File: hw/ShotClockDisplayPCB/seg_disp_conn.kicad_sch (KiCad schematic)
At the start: 4 parts, among them J2 Conn_01x05_Socket, J3 Conn_01x05_Socket, J4 Conn_01x05_Socket, J5 Conn_01x05_Socket

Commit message: Finshed both schematics
- LED driving transistors are placed
- All connectors on segment display PCB are placed
- All schematic references have been re-configured (autosort on Y axis)
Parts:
- renumbered J4 to J3, J3 to J4
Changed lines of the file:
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@@
       (project "ShotClockDisplayPCB"
         (path "/baf3f1b3-1588-4756-b7d1-50b7c58bafb0/06b39ac0-a89e-4700-88fa-059ca62688ec"
-          (reference "#PWR03") (unit 1)
+          (reference "#PWR025") (unit 1)
         )
       )
@@
       (project "ShotClockDisplayPCB"
         (path "/baf3f1b3-1588-4756-b7d1-50b7c58bafb0/06b39ac0-a89e-4700-88fa-059ca62688ec"
-          (reference "#PWR04") (unit 1)
+          (reference "#PWR026") (unit 1)
         )
       )
@@
   (symbol (lib_id "Connector:Conn_01x05_Socket") (at 180.34 80.01 0) (unit 1)
     (in_bom yes) (on_board yes) (dnp no)
-    (property "Reference" "J4" (at 181.61 78.74 0)
+    (property "Reference" "J3" (at 181.61 78.74 0)
       (effects (font (size 1.27 1.27)) (justify left))
     )
@@
       (project "ShotClockDisplayPCB"
         (path "/baf3f1b3-1588-4756-b7d1-50b7c58bafb0/06b39ac0-a89e-4700-88fa-059ca62688ec"
-          (reference "J4") (unit 1)
+          (reference "J3") (unit 1)
         )
       )
@@
   (symbol (lib_id "Connector:Conn_01x05_Socket") (at 118.11 97.79 0) (unit 1)
     (in_bom yes) (on_board yes) (dnp no)
-    (property "Reference" "J3" (at 119.38 96.52 0)
+    (property "Reference" "J4" (at 119.38 96.52 0)
       (effects (font (size 1.27 1.27)) (justify left))
     )
@@
       (project "ShotClockDisplayPCB"
         (path "/baf3f1b3-1588-4756-b7d1-50b7c58bafb0/06b39ac0-a89e-4700-88fa-059ca62688ec"
-          (reference "J3") (unit 1)
+          (reference "J4") (unit 1)
         )
       )

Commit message: Display print
Changed mainboard connector to FPC connector
Created routing for board
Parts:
- renumbered J2 to J1, J3 to J2, J4 to J3, J5 to J4
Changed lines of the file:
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@@
   (symbol (lib_id "Connector:Conn_01x05_Socket") (at 118.11 80.01 0) (unit 1)
     (in_bom yes) (on_board yes) (dnp no)
-    (property "Reference" "J2" (at 119.38 78.74 0)
+    (property "Reference" "J1" (at 119.38 78.74 0)
       (effects (font (size 1.27 1.27)) (justify left))
     )
@@
       (project "ShotClockDisplayPCB"
         (path "/baf3f1b3-1588-4756-b7d1-50b7c58bafb0/06b39ac0-a89e-4700-88fa-059ca62688ec"
-          (reference "J2") (unit 1)
+          (reference "J1") (unit 1)
         )
       )
@@
   (symbol (lib_id "Connector:Conn_01x05_Socket") (at 180.34 80.01 0) (unit 1)
     (in_bom yes) (on_board yes) (dnp no)
-    (property "Reference" "J3" (at 181.61 78.74 0)
+    (property "Reference" "J2" (at 181.61 78.74 0)
       (effects (font (size 1.27 1.27)) (justify left))
     )
@@
       (project "ShotClockDisplayPCB"
         (path "/baf3f1b3-1588-4756-b7d1-50b7c58bafb0/06b39ac0-a89e-4700-88fa-059ca62688ec"
-          (reference "J3") (unit 1)
+          (reference "J2") (unit 1)
         )
       )
@@
   (symbol (lib_id "Connector:Conn_01x05_Socket") (at 180.34 97.79 0) (unit 1)
     (in_bom yes) (on_board yes) (dnp no)
-    (property "Reference" "J5" (at 181.61 96.52 0)
+    (property "Reference" "J4" (at 181.61 96.52 0)
       (effects (font (size 1.27 1.27)) (justify left))
     )
@@
       (project "ShotClockDisplayPCB"
         (path "/baf3f1b3-1588-4756-b7d1-50b7c58bafb0/06b39ac0-a89e-4700-88fa-059ca62688ec"
-          (reference "J5") (unit 1)
+          (reference "J4") (unit 1)
         )
       )
@@
   (symbol (lib_id "Connector:Conn_01x05_Socket") (at 118.11 97.79 0) (unit 1)
     (in_bom yes) (on_board yes) (dnp no)
-    (property "Reference" "J4" (at 119.38 96.52 0)
+    (property "Reference" "J3" (at 119.38 96.52 0)
       (effects (font (size 1.27 1.27)) (justify left))
     )
@@
       (project "ShotClockDisplayPCB"
         (path "/baf3f1b3-1588-4756-b7d1-50b7c58bafb0/06b39ac0-a89e-4700-88fa-059ca62688ec"
-          (reference "J4") (unit 1)
+          (reference "J3") (unit 1)
         )
       )

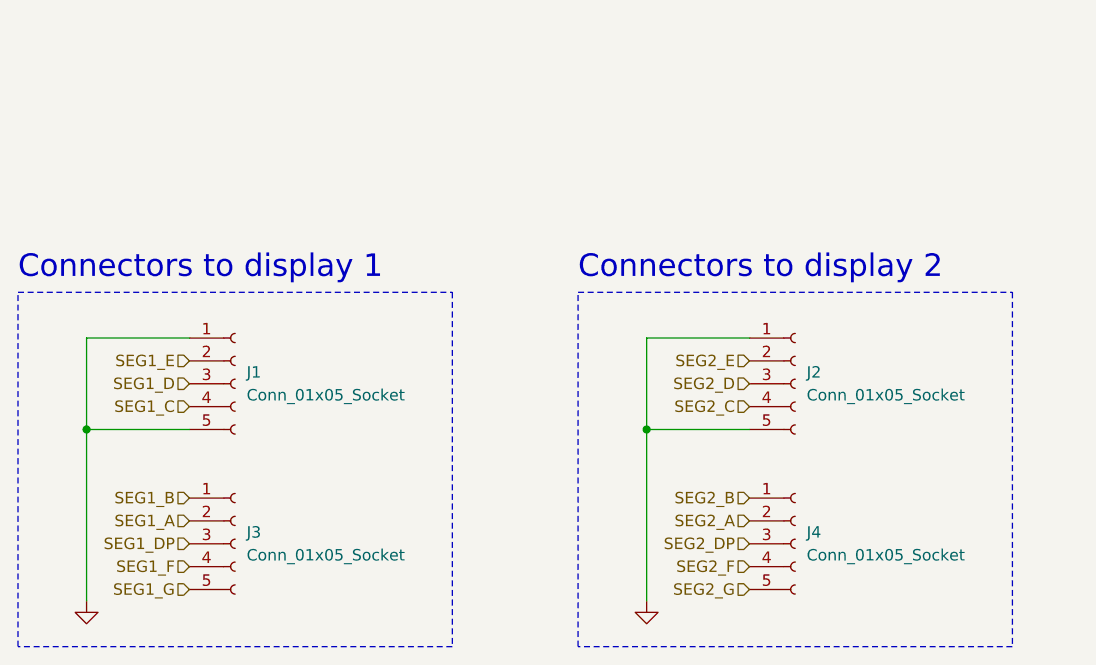
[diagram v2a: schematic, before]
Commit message: Started on display board rework
added new footprints
added HW select shunts/jumpers
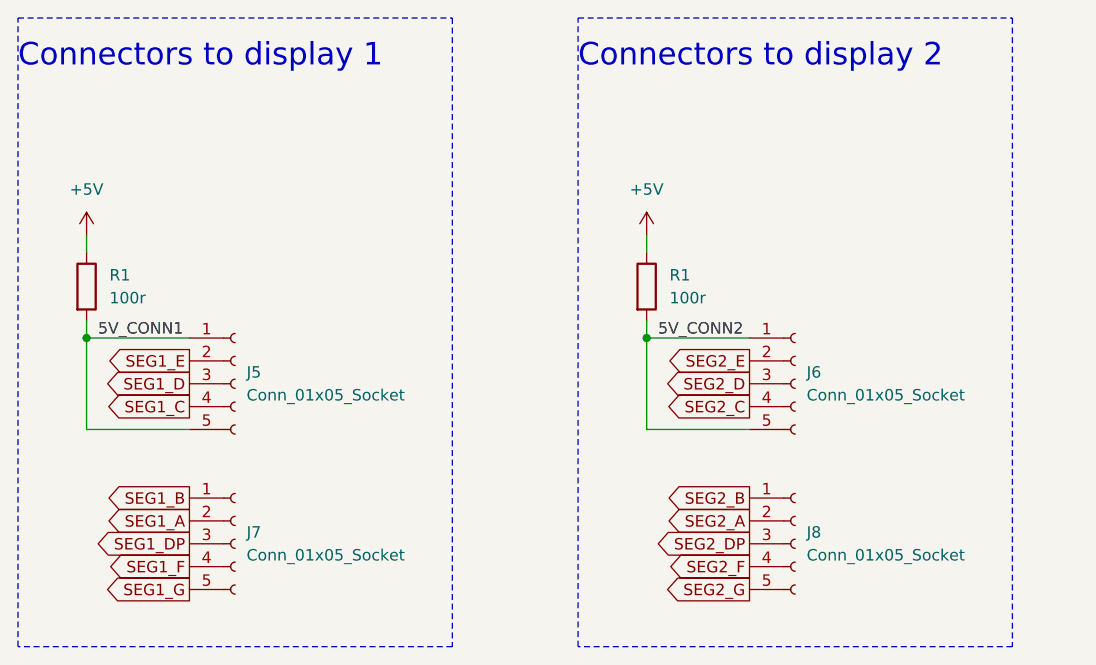
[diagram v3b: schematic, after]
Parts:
- added R1 (x2): 100r, Resistor_SMD:R_0402_1005Metric, symbol Device:R
- renumbered J1 to J5, J2 to J6, J3 to J7, J4 to J8
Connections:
- net GND renamed 5V_CONN1
- net 5V_CONN1: now also R1.2; no longer J6.1 (Pin_1), J6.5 (Pin_5)
- new net +5V: R1.1, R1.1
- new net 5V_CONN2: J6.1 (Pin_1), J6.5 (Pin_5), R1.2

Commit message: Changed LCSC Part numbers for disp board
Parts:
- J5, J6, J7, J8: LCSC Part (none) -> C2897368
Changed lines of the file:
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@@
+      (effects (font (size 1.27 1.27)) hide)
+    )
+    (property "LCSC Part" "C2897368" (at 118.11 80.01 0)
       (effects (font (size 1.27 1.27)) hide)
     )
@@
       (effects (font (size 1.27 1.27)) hide)
     )
+    (property "LCSC Part" "C2897368" (at 180.34 80.01 0)
+      (effects (font (size 1.27 1.27)) hide)
+    )
     (pin "1")
     (pin "2")
@@
     )
     (property "Datasheet" "~" (at 180.34 97.79 0)
+      (effects (font (size 1.27 1.27)) hide)
+    )
+    (property "LCSC Part" "C2897368" (at 180.34 97.79 0)
       (effects (font (size 1.27 1.27)) hide)
     )
@@
       (effects (font (size 1.27 1.27)) hide)
     )
+    (property "LCSC Part" "C2897368" (at 118.11 97.79 0)
+      (effects (font (size 1.27 1.27)) hide)
+    )

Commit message: Fixed mainboard with feedback from Luc
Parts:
- R1: footprint Resistor_SMD:R_0402_1005Metric -> Resistor_SMD:R_1210_3225Metric
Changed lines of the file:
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@@
       (effects (font (size 1.27 1.27)) (justify left))
     )
-    (property "Footprint" "Resistor_SMD:R_0402_1005Metric" (at 162.052 69.215 90)
+    (property "Footprint" "Resistor_SMD:R_1210_3225Metric" (at 162.052 69.215 90)
       (effects (font (size 1.27 1.27)) hide)
     )
@@
       (effects (font (size 1.27 1.27)) (justify left))
     )
-    (property "Footprint" "Resistor_SMD:R_0402_1005Metric" (at 99.822 69.215 90)
+    (property "Footprint" "Resistor_SMD:R_1210_3225Metric" (at 99.822 69.215 90)
       (effects (font (size 1.27 1.27)) hide)
     )

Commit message: REV2 Finished
Corrected LCSC part number
Added polarities on silkscreen
Made output files for both boards
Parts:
- R1: LCSC Part C25076 -> C2933827
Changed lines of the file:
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@@
       (effects (font (size 1.27 1.27)) hide)
     )
-    (property "LCSC Part" "C25076" (at 163.83 69.215 0)
+    (property "LCSC Part" "C2933827" (at 163.83 69.215 0)
       (effects (font (size 1.27 1.27)) hide)
     )
@@
       (effects (font (size 1.27 1.27)) hide)
     )
-    (property "LCSC Part" "C25076" (at 101.6 69.215 0)
+    (property "LCSC Part" "C2933827" (at 101.6 69.215 0)
       (effects (font (size 1.27 1.27)) hide)
     )
